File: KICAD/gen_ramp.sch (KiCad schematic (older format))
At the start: 12 parts

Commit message: a ton of new stuff. V0.8
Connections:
- net 2.9V: now reaches R?.1, R?.2, U?.2 (-)
- net 3.5V: now reaches R?.1, R?.2, U?.5 (+)
- net +7V renamed VCC
- net VCC: no longer R?.2, R?.2
- new net VREF: R?.2, R?.2
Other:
- note added: "A verifier !"
- note added: "Choisir AOP Rail To Rail\nDefinir Resistances & Condos"
- note added: "Offset Integrateur"
- note added: "Offset Trigger"
- note added: "Slew rate > ?\nAlim au moins a 7v"
- note removed: "double offset ?"
- moved on the sheet: C?, R?, U?B
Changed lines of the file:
@@
 $Descr A4 11693 8268
 encoding utf-8
-Sheet 2 15
+Sheet 2 16
 Title "SESAME"
 Date ""
 Rev ""
 Comp "ALEEA"
-Comment1 ""
+Comment1 "Dessin : Kevin & Guillaume Arthaud"
 Comment2 ""
 Comment3 ""
 Comment4 ""
 $EndDescr
-Text HLabel 8900 3650 2    50   Output ~ 0
+Text HLabel 8000 3650 2    50   Output ~ 0
 Ramp
 $Comp
@@
 L Amplifier_Operational:LM7332 U?
 U 2 1 610B1F20
-P 7350 3650
-F 0 "U?" H 7350 3283 50  0000 C CNN
-F 1 "LM7332" H 7350 3374 50  0000 C CNN
-F 2 "" H 7350 3650 50  0001 C CNN
-F 3 "http://www.ti.com/lit/ds/symlink/lm7332.pdf" H 7350 3650 50  0001 C CNN
-	2    7350 3650
+P 7000 3650
+F 0 "U?" H 7000 3283 50  0000 C CNN
+F 1 "LM7332" H 7000 3374 50  0000 C CNN
+F 2 "" H 7000 3650 50  0001 C CNN
+F 3 "http://www.ti.com/lit/ds/symlink/lm7332.pdf" H 7000 3650 50  0001 C CNN
+	2    7000 3650
 	1    0    0    1
 $EndComp
 $Comp
-L power:GND #PWR?
+L power:GND #PWR0102
 U 1 1 610B3256
 P 3150 4000
-F 0 "#PWR?" H 3150 3750 50  0001 C CNN
+F 0 "#PWR0102" H 3150 3750 50  0001 C CNN
 F 1 "GND" H 3155 3827 50  0000 C CNN
 F 2 "" H 3150 4000 50  0001 C CNN
@@
 L Device:R R?
 U 1 1 611047CD
-P 6650 3550
-F 0 "R?" V 6443 3550 50  0000 C CNN
-F 1 "R" V 6534 3550 50  0000 C CNN
-F 2 "" V 6580 3550 50  0001 C CNN
-F 3 "~" H 6650 3550 50  0001 C CNN
-	1    6650 3550
+P 6300 3550
+F 0 "R?" V 6093 3550 50  0000 C CNN
+F 1 "R" V 6184 3550 50  0000 C CNN
+F 2 "" V 6230 3550 50  0001 C CNN
+F 3 "~" H 6300 3550 50  0001 C CNN
+	1    6300 3550
 	0    1    1    0
 $EndComp
@@
 L Device:R R?
 U 1 1 6110CE49
-P 3150 5150
-F 0 "R?" H 3080 5104 50  0000 R CNN
-F 1 "R" H 3080 5195 50  0000 R CNN
-F 2 "" V 3080 5150 50  0001 C CNN
-F 3 "~" H 3150 5150 50  0001 C CNN
-	1    3150 5150
+P 5900 5100
+F 0 "R?" H 5830 5054 50  0000 R CNN
+F 1 "R" H 5830 5145 50  0000 R CNN
+F 2 "" V 5830 5100 50  0001 C CNN
+F 3 "~" H 5900 5100 50  0001 C CNN
+	1    5900 5100
 	-1   0    0    1
 $EndComp
 Wire Wire Line
-	6950 3750 7050 3750
-$Comp
-L power:GND #PWR?
+	6600 3750 6700 3750
+$Comp
+L power:GND #PWR0103
 U 1 1 611134C1
-P 3150 5300
-F 0 "#PWR?" H 3150 5050 50  0001 C CNN
-F 1 "GND" H 3155 5127 50  0000 C CNN
-F 2 "" H 3150 5300 50  0001 C CNN
-F 3 "" H 3150 5300 50  0001 C CNN
-	1    3150 5300
+P 5900 5250
+F 0 "#PWR0103" H 5900 5000 50  0001 C CNN
+F 1 "GND" H 5905 5077 50  0000 C CNN
+F 2 "" H 5900 5250 50  0001 C CNN
+F 3 "" H 5900 5250 50  0001 C CNN
+	1    5900 5250
 	1    0    0    -1
 $EndComp
@@
 L Device:C C?
 U 1 1 611171B1
-P 7350 3050
-F 0 "C?" V 7098 3050 50  0000 C CNN
-F 1 "C" V 7189 3050 50  0000 C CNN
-F 2 "" H 7388 2900 50  0001 C CNN
-F 3 "~" H 7350 3050 50  0001 C CNN
-	1    7350 3050
+P 7000 3050
+F 0 "C?" V 6748 3050 50  0000 C CNN
+F 1 "C" V 6839 3050 50  0000 C CNN
+F 2 "" H 7038 2900 50  0001 C CNN
+F 3 "~" H 7000 3050 50  0001 C CNN
+	1    7000 3050
 	0    1    1    0
 $EndComp
 Wire Wire Line
-	7200 3050 6950 3050
-Wire Wire Line
-	7500 3050 7750 3050
-Wire Wire Line
-	7650 3650 7750 3650
+	6850 3050 6600 3050
+Wire Wire Line
+	7150 3050 7400 3050
+Wire Wire Line
+	7300 3650 7400 3650
 Wire Wire Line
 	4150 3450 3750 3450
@@
 	3750 3450 3750 2500
 Wire Wire Line
-	3750 2500 8150 2500
+	3750 2500 7800 2500
 $Comp
 L Amplifier_Operational:LM7332 U?
@@
 P 1350 7400
 AR Path="/60F2F8DD/610F3596" Ref="#PWR?"  Part="1"
-AR Path="/60F16FAE/610F3596" Ref="#PWR?"  Part="1"
-F 0 "#PWR?" H 1350 7150 50  0001 C CNN
+AR Path="/60F16FAE/610F3596" Ref="#PWR0105"  Part="1"
+F 0 "#PWR0105" H 1350 7150 50  0001 C CNN
 F 1 "GND" H 1355 7227 50  0000 C CNN
 F 2 "" H 1350 7400 50  0001 C CNN
@@
 Connection ~ 5450 3550
 Wire Wire Line
-	5450 3550 6500 3550
+	5450 3550 6150 3550
 Wire Wire Line
 	4900 3050 4650 3050
@@
 	4650 3450 4750 3450
 Wire Wire Line
-	6950 3550 6950 3050
-Connection ~ 6950 3550
-Wire Wire Line
-	6950 3550 7050 3550
-Wire Wire Line
-	6800 3550 6950 3550
-Wire Wire Line
-	7750 3650 7750 3050
-Connection ~ 7750 3650
-Wire Wire Line
-	7750 3650 8150 3650
-Wire Wire Line
-	3150 5000 3150 4950
-Wire Wire Line
-	3150 4950 6950 4950
-Wire Wire Line
-	6950 3750 6950 4950
-Connection ~ 3150 4950
-Wire Wire Line
-	3150 4950 3150 4900
+	6600 3550 6600 3050
+Connection ~ 6600 3550
+Wire Wire Line
+	6600 3550 6700 3550
+Wire Wire Line
+	6450 3550 6600 3550
+Wire Wire Line
+	7400 3650 7400 3050
+Connection ~ 7400 3650
+Wire Wire Line
+	7400 3650 7800 3650
+Wire Wire Line
+	6600 3750 6600 4900
 $Comp
 L Device:R R?
@@
 L Device:R R?
 U 1 1 6111A906
-P 3150 4750
-F 0 "R?" H 3080 4704 50  0000 R CNN
-F 1 "R" H 3080 4795 50  0000 R CNN
-F 2 "" V 3080 4750 50  0001 C CNN
-F 3 "~" H 3150 4750 50  0001 C CNN
-	1    3150 4750
+P 5900 4700
+F 0 "R?" H 5830 4654 50  0000 R CNN
+F 1 "R" H 5830 4745 50  0000 R CNN
+F 2 "" V 5830 4700 50  0001 C CNN
+F 3 "~" H 5900 4700 50  0001 C CNN
+	1    5900 4700
 	-1   0    0    1
 $EndComp
@@
 	5650 2700 5650 4150
 Wire Notes Line
-	7950 2700 7950 4150
+	7600 2700 7600 4150
 Wire Notes Line
 	3950 4150 3950 2700
@@
 	3950 2700 5650 2700
 Wire Notes Line
-	6300 4150 6300 2700
-Wire Notes Line
-	6300 4150 7950 4150
-Wire Notes Line
-	6300 2700 7950 2700
-Wire Wire Line
-	8150 2500 8150 3650
-Connection ~ 8150 3650
-Wire Wire Line
-	8150 3650 8900 3650
-Text Notes 7500 4100 0    50   ~ 0
+	5950 4150 5950 2700
+Wire Notes Line
+	5950 4150 7600 4150
+Wire Notes Line
+	5950 2700 7600 2700
+Wire Wire Line
+	7800 2500 7800 3650
+Connection ~ 7800 3650
+Wire Wire Line
+	7800 3650 8000 3650
+Text Notes 7150 4100 0    50   ~ 0
 Integrateur
 Text Notes 5050 4100 0    50   ~ 0
 Schmitt trigger
-$Comp
-L Sesame:+7V #PWR?
-U 1 1 6129F143
+Wire Notes Line
+	5600 4300 6450 4300
+Wire Notes Line
+	6450 4300 6450 5750
+Wire Notes Line
+	6450 5750 5600 5750
+Wire Notes Line
+	5600 5750 5600 4300
+Text Notes 5700 5700 0    50   ~ 0
+Offset Integrateur
+Text Label 6100 4900 0    50   ~ 0
+3.5V
+Text Label 3350 3650 0    50   ~ 0
+2.9V
+Text Notes 3300 3750 0    50   ~ 10
+A verifier !
+Wire Wire Line
+	5900 4850 5900 4900
+Wire Wire Line
+	6600 4900 5900 4900
+Connection ~ 5900 4900
+Wire Wire Line
+	5900 4900 5900 4950
+Text Notes 4700 2400 0    100  ~ 20
+Choisir AOP Rail To Rail\nDefinir Resistances & Condos
+Text Notes 4100 3900 0    50   ~ 0
+Slew rate > ?\nAlim au moins a 7v
+Wire Notes Line
+	2950 3050 3550 3050
+Wire Notes Line
+	3550 3050 3550 4350
+Wire Notes Line
+	3550 4350 2950 4350
+Wire Notes Line
+	2950 4350 2950 3050
+Text Notes 3000 4300 0    50   ~ 0
+Offset Trigger
+$Comp
+L Sesame:VREF #PWR0107
+U 1 1 6155084A
+P 3150 3300
+F 0 "#PWR0107" H 3150 3150 50  0001 C CNN
+F 1 "VREF" H 3165 3473 50  0000 C CNN
+F 2 "" H 3150 3300 50  0001 C CNN
+F 3 "" H 3150 3300 50  0001 C CNN
+	1    3150 3300
+	1    0    0    -1
+$EndComp
+$Comp
+L Sesame:VREF #PWR0110
+U 1 1 615517F7
+P 5900 4550
+F 0 "#PWR0110" H 5900 4400 50  0001 C CNN
+F 1 "VREF" H 5915 4723 50  0000 C CNN
+F 2 "" H 5900 4550 50  0001 C CNN
+F 3 "" H 5900 4550 50  0001 C CNN
+	1    5900 4550
+	1    0    0    -1
+$EndComp
+$Comp
+L power:VCC #PWR0111
+U 1 1 6155377F
 P 1350 6550
-F 0 "#PWR?" H 1350 6400 50  0001 C CNN
-F 1 "+7V" H 1365 6723 50  0000 C CNN
+F 0 "#PWR0111" H 1350 6400 50  0001 C CNN
+F 1 "VCC" H 1365 6723 50  0000 C CNN
 F 2 "" H 1350 6550 50  0001 C CNN
 F 3 "" H 1350 6550 50  0001 C CNN
@@
 	1    0    0    -1
 $EndComp
-$Comp
-L Sesame:+7V #PWR?
-U 1 1 612A0A89
-P 3150 4600
-F 0 "#PWR?" H 3150 4450 50  0001 C CNN
-F 1 "+7V" H 3165 4773 50  0000 C CNN
-F 2 "" H 3150 4600 50  0001 C CNN
-F 3 "" H 3150 4600 50  0001 C CNN
-	1    3150 4600
-	1    0    0    -1
-$EndComp
-$Comp
-L Sesame:+7V #PWR?
-U 1 1 612A1435
-P 3150 3300
-F 0 "#PWR?" H 3150 3150 50  0001 C CNN
-F 1 "+7V" H 3165 3473 50  0000 C CNN
-F 2 "" H 3150 3300 50  0001 C CNN
-F 3 "" H 3150 3300 50  0001 C CNN
-	1    3150 3300
-	1    0    0    -1
-$EndComp
-Wire Notes Line
-	2850 2950 3700 2950
-Wire Notes Line
-	3700 2950 3700 5800
-Wire Notes Line
-	3700 5800 2850 5800
-Wire Notes Line
-	2850 5800 2850 2950
-Text Notes 2950 5750 0    50   ~ 10
-double offset ?
 $EndSCHEMATC

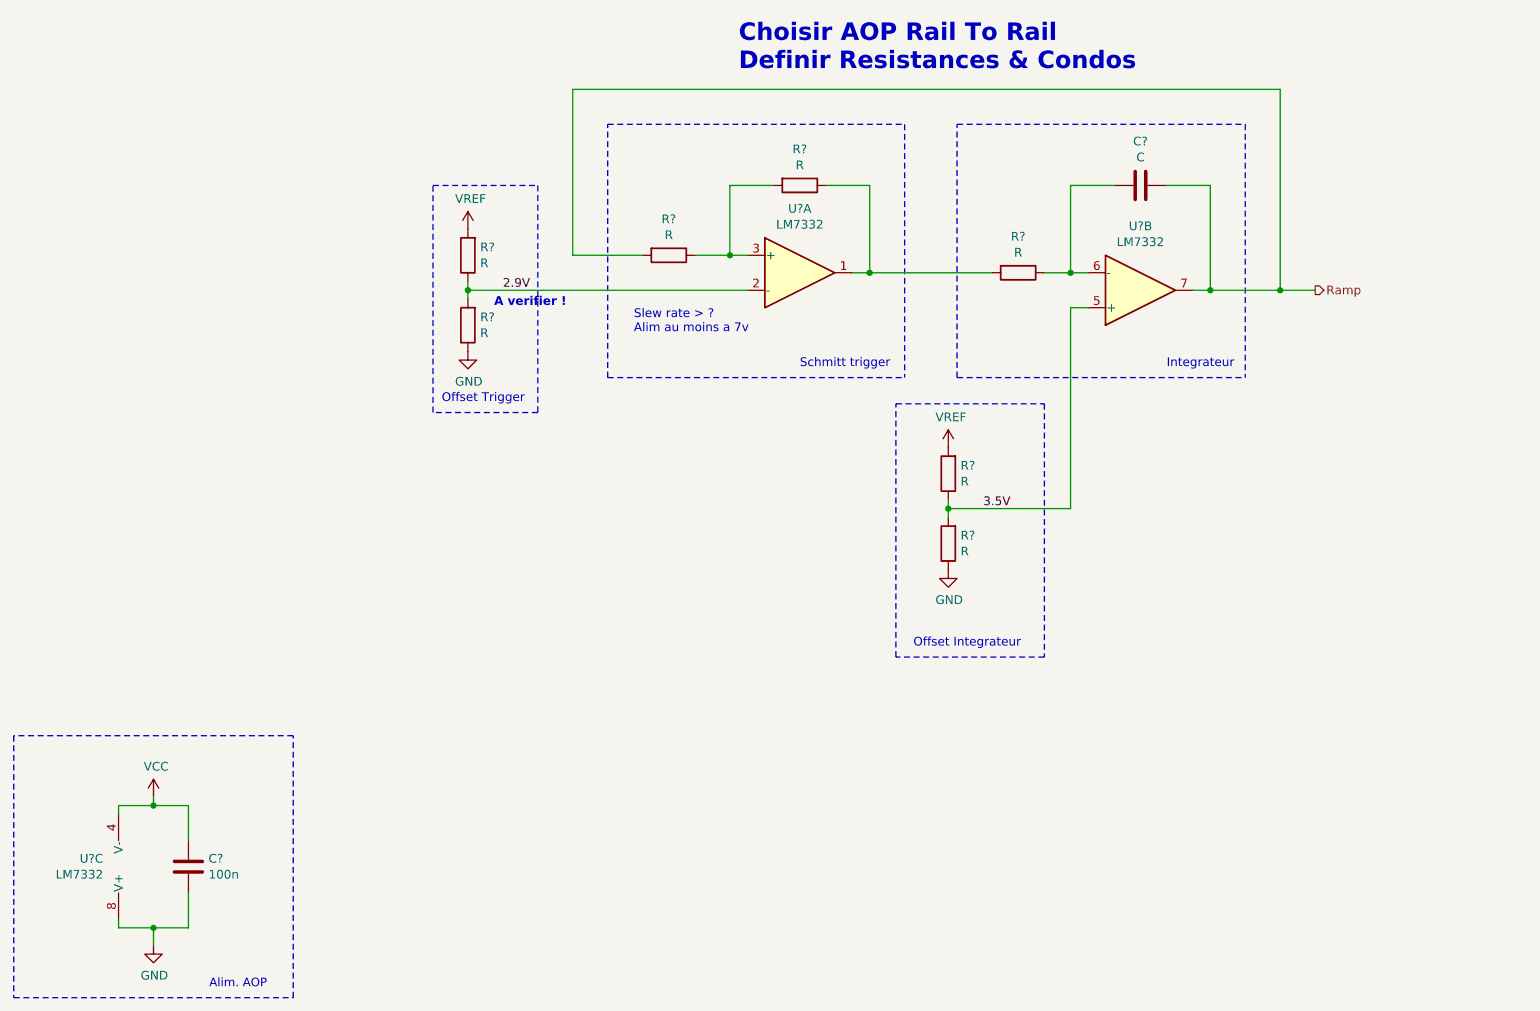
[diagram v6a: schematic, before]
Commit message: PID + PWM + RAMP finished
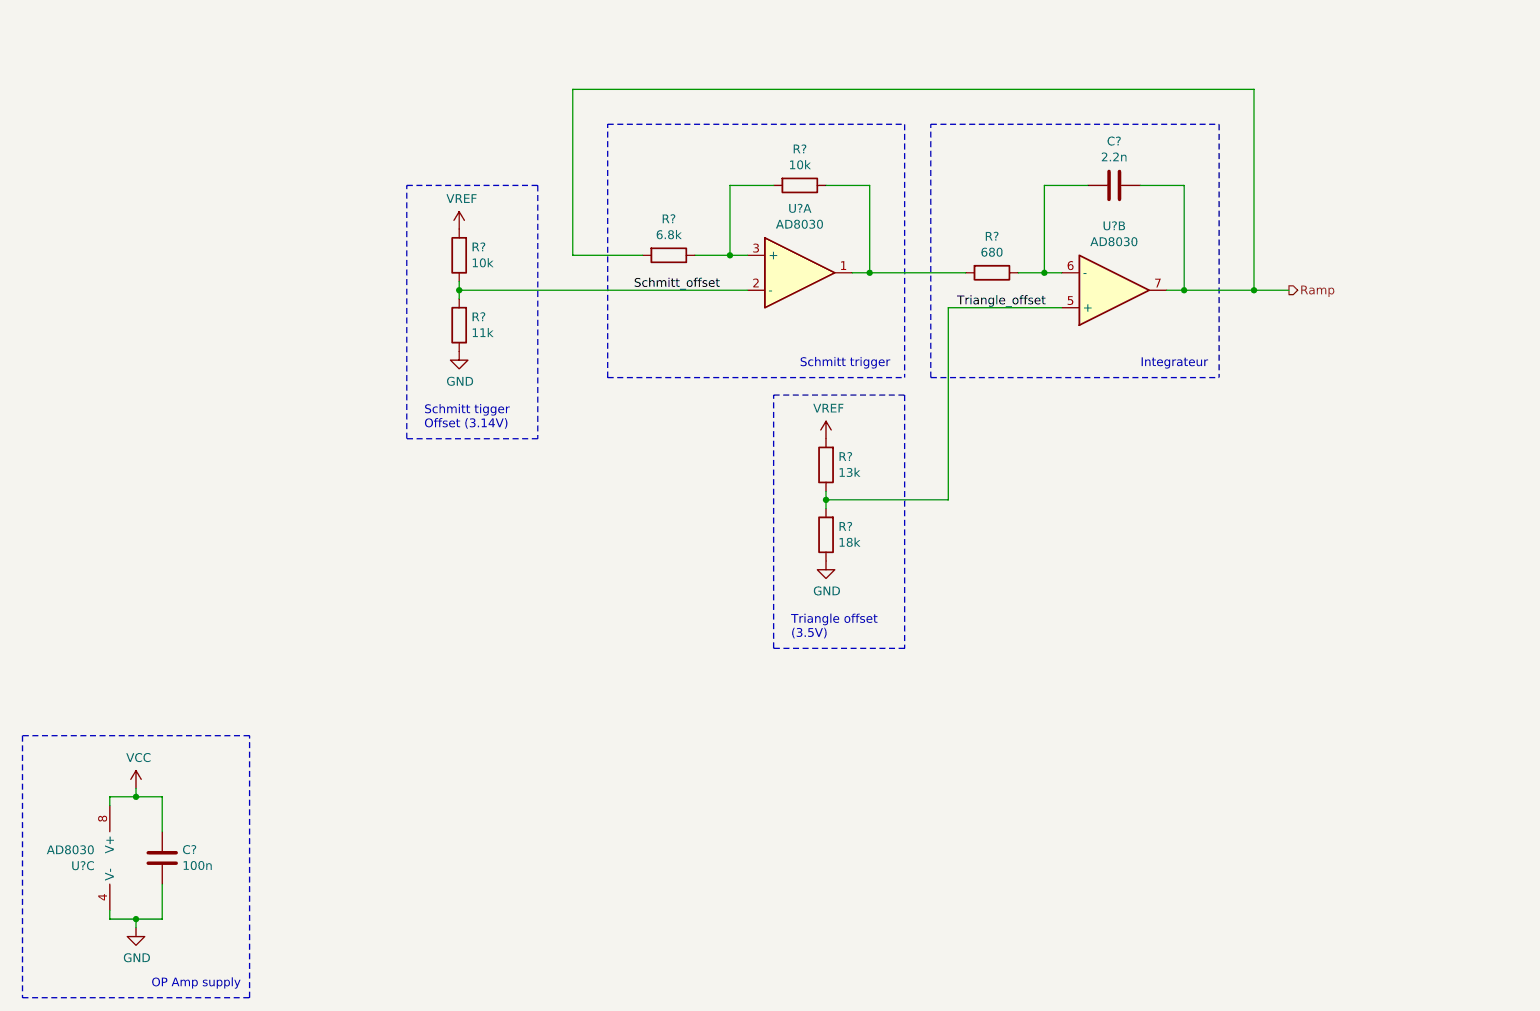
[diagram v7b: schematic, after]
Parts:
- removed C?: 100n, symbol Device:C
- removed R? (x2): R, symbol Device:R
- removed U? (x3): LM7332, symbol Amplifier_Operational:LM7332
- added C?: 100n, symbol Device:C
- added R?: 11k, Resistor_SMD:R_0805_2012Metric_Pad1.15x1.40mm_HandSolder, symbol Device:R
- added R?: 10k, Resistor_SMD:R_0805_2012Metric_Pad1.15x1.40mm_HandSolder, symbol Device:R
- added U? (x3): AD8030, symbol Sesame:AD8030
- C?: value C -> 2.2n; footprint (none) -> Capacitor_SMD:C_0805_2012Metric_Pad1.15x1.40mm_HandSolder
- R?: value R -> 6.8k; footprint (none) -> Resistor_SMD:R_0805_2012Metric_Pad1.15x1.40mm_HandSolder
- R?: value R -> 10k; footprint (none) -> Resistor_SMD:R_0805_2012Metric_Pad1.15x1.40mm_HandSolder
- R?: value R -> 680; footprint (none) -> Resistor_SMD:R_0805_2012Metric_Pad1.15x1.40mm_HandSolder
- R?: value R -> 18k; footprint (none) -> Resistor_SMD:R_0805_2012Metric_Pad1.15x1.40mm_HandSolder
- R?: value R -> 13k; footprint (none) -> Resistor_SMD:R_0805_2012Metric_Pad1.15x1.40mm_HandSolder
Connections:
- net GND: now also C?.2, R?.1, U?.4 (V-)
- net Ramp: now also U?.7
- net VCC: now also C?.1, U?.8 (V+)
- net VREF: now also R?.2
- net at R?.1, R?.2: now also U?.1
- net at R?.1, R?.2: now also U?.3 (+)
- net at C?.2, R?.1: now also U?.6 (-)
- net 3.5V renamed Triangle_offset
- net Triangle_offset: now also U?.5 (+)
- new net Schmitt_offset: R?.1, R?.2, U?.2 (-)
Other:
- note added: "OP Amp supply"
- note added: "Schmitt tigger \nOffset (3.14V)"
- note added: "Triangle offset\n(3.5V)"
- note removed: "A verifier !"
- note removed: "Alim. AOP"
- note removed: "Choisir AOP Rail To Rail\nDefinir Resistances & Condos"
- note removed: "Offset Integrateur"
- note removed: "Offset Trigger"
- note removed: "Slew rate > ?\nAlim au moins a 7v"
- moved on the sheet: C?, R?

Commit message: mainly footprints
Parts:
- U2: renamed from U?; footprint (none) -> Package_SO:SO-8_3.9x4.9mm_P1.27mm
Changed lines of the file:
@@
 $Descr A4 11693 8268
 encoding utf-8
-Sheet 16 16
+Sheet 9 16
 Title "SESAME"
 Date ""
@@
 AR Path="/60F1AF26/61324C80" Ref="U?"  Part="3"
 AR Path="/60F1B237/61324C80" Ref="U?"  Part="3"
-AR Path="/60F16FAE/61324C80" Ref="U?"  Part="3"
-F 0 "U?" H 1013 6854 50  0000 R CNN
+AR Path="/60F16FAE/61324C80" Ref="U2"  Part="3"
+F 0 "U2" H 1013 6854 50  0000 R CNN
 F 1 "AD8030" H 1013 6945 50  0000 R CNN
-F 2 "" H 1200 6900 50  0001 C CNN
+F 2 "Package_SO:SO-8_3.9x4.9mm_P1.27mm" H 1200 6900 50  0001 C CNN
 F 3 "~" H 1200 6900 50  0001 C CNN
 	3    1200 6900
@@
 $EndComp
 $Comp
-L Sesame:AD8030 U?
+L Sesame:AD8030 U2
 U 2 1 6132B377
 P 6850 3650
-F 0 "U?" H 6850 3283 50  0000 C CNN
+F 0 "U2" H 6850 3283 50  0000 C CNN
 F 1 "AD8030" H 6850 3374 50  0000 C CNN
-F 2 "" H 6850 3650 50  0001 C CNN
+F 2 "Package_SO:SO-8_3.9x4.9mm_P1.27mm" H 6850 3650 50  0001 C CNN
 F 3 "~" H 6850 3650 50  0001 C CNN
 	2    6850 3650
@@
 $EndComp
 $Comp
-L Sesame:AD8030 U?
+L Sesame:AD8030 U2
 U 1 1 6132F06A
 P 5050 3550
-F 0 "U?" H 5050 3917 50  0000 C CNN
+F 0 "U2" H 5050 3917 50  0000 C CNN
 F 1 "AD8030" H 5050 3826 50  0000 C CNN
-F 2 "" H 5050 3550 50  0001 C CNN
+F 2 "Package_SO:SO-8_3.9x4.9mm_P1.27mm" H 5050 3550 50  0001 C CNN
 F 3 "~" H 5050 3550 50  0001 C CNN
 	1    5050 3550
